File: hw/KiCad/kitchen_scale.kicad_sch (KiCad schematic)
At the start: 11 parts, among them J1 Conn_01x08_Socket, J2 Conn_HX711, SW1 SW_Push, SW2 SW_SPST, SW3 SW_Push, SW4 SW_Push, U1 DEBO1_3_7LI_1_0A charge_contr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, U2 WeMos_D1_mini, U3 LF33_TO220

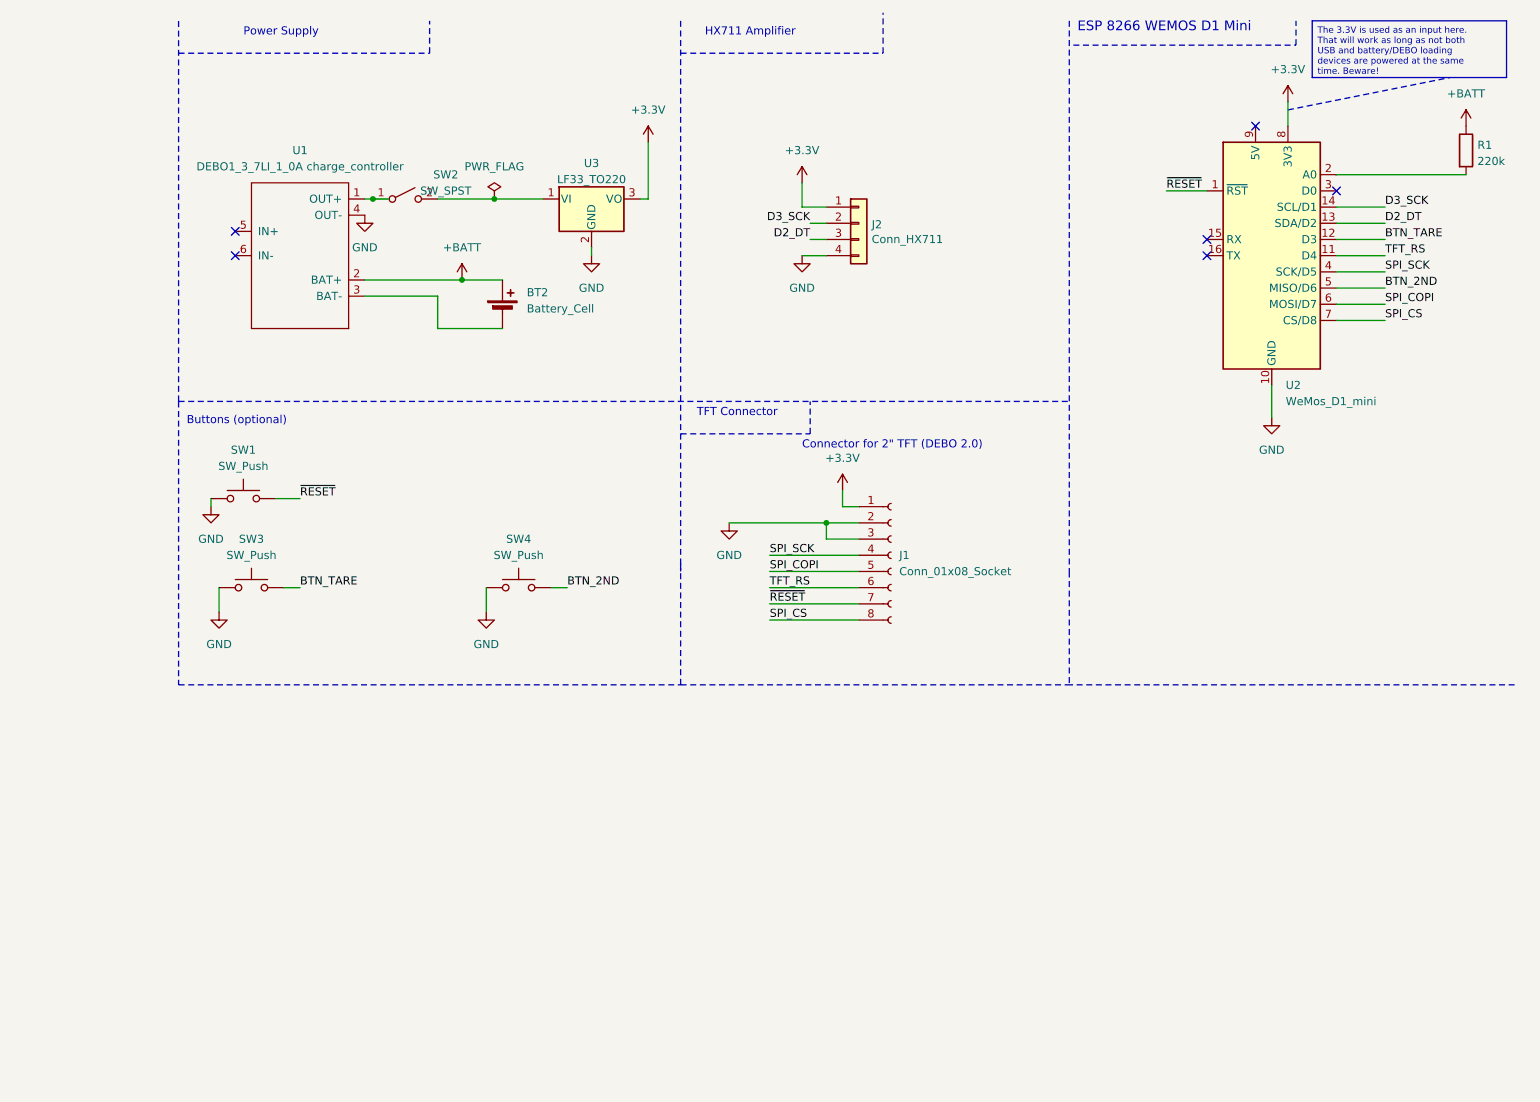
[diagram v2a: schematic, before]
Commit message: Add footprints Add first draft of PCB
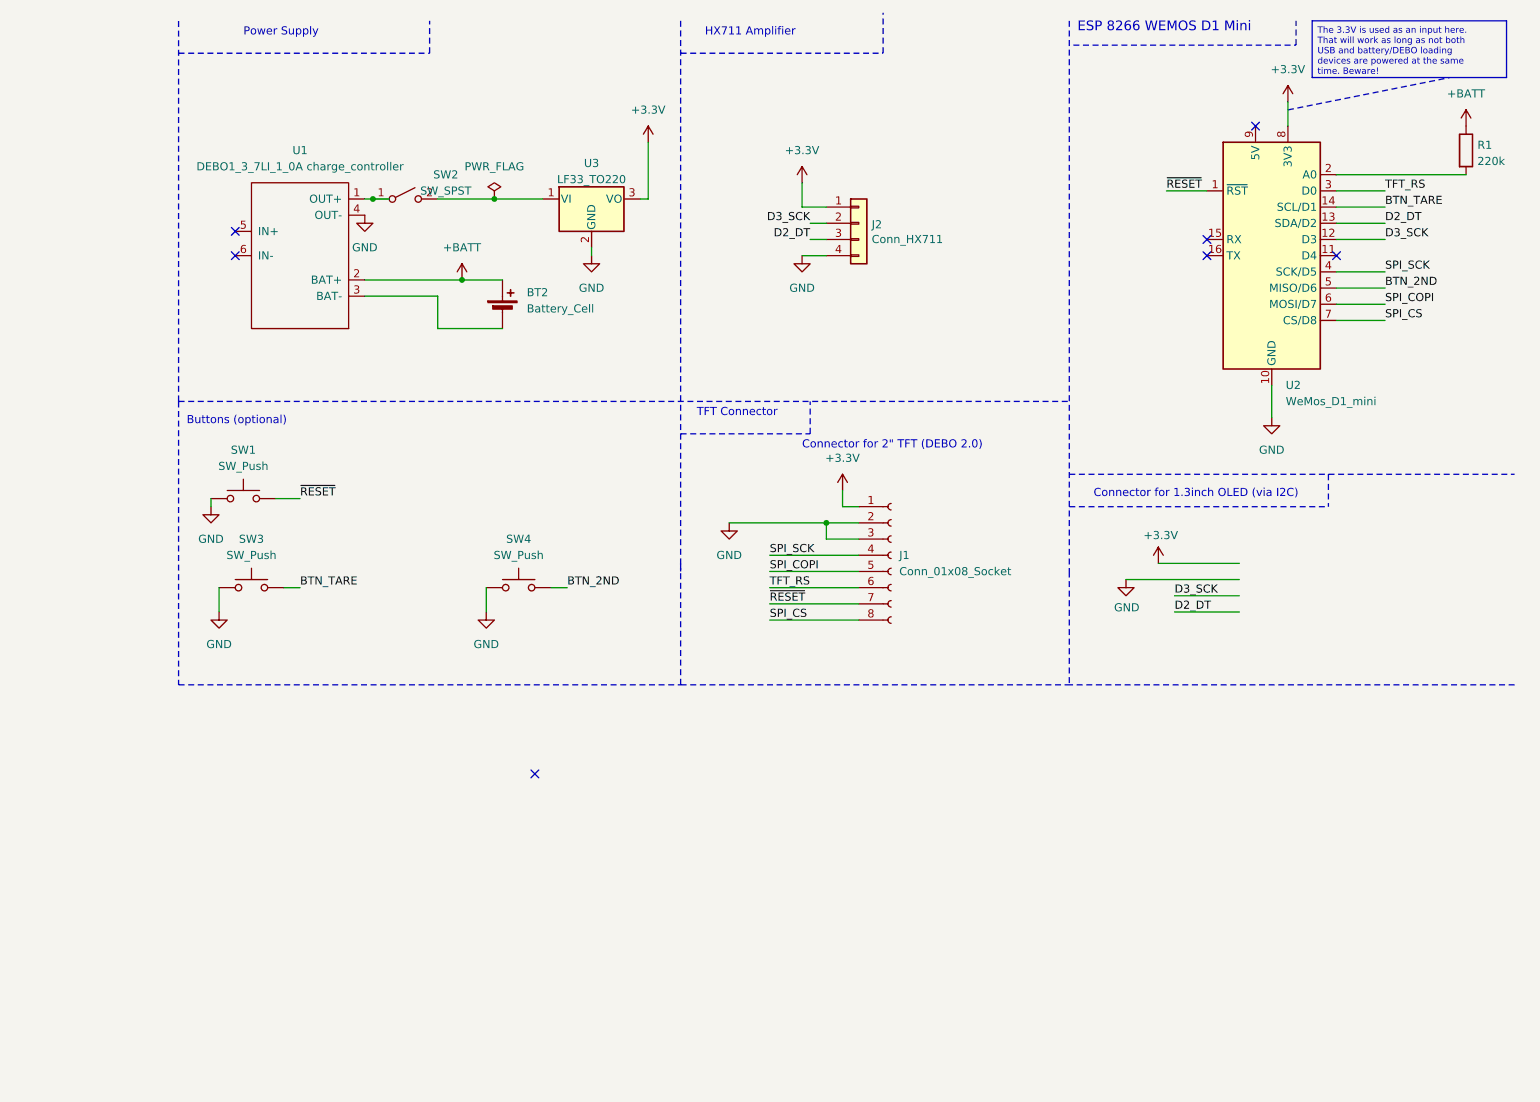
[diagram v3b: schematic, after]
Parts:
- BT2: footprint (none) -> Connector_PinHeader_2.54mm:PinHeader_1x02_P2.54mm_Vertical
- J1: footprint (none) -> Connector_PinHeader_2.54mm:PinHeader_2x04_P2.54mm_Vertical
- J2: footprint (none) -> Connector_PinSocket_2.54mm:PinSocket_1x04_P2.54mm_Vertical
- SW1, SW3, SW4: footprint (none) -> Button_Switch_THT:SW_PUSH-12mm
- SW2: footprint (none) -> Connector_PinSocket_2.54mm:PinSocket_1x02_P2.54mm_Vertical
- U1: footprint (none) -> Mine:DEBO1_3_7LI_1_0A_charge_controller
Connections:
- net BTN_TARE: now also U2.14 (SCL/D1); no longer U2.12 (D3)
- net D3_SCK: now also U2.12 (D3); no longer U2.14 (SCL/D1)
- net TFT_RS: now also U2.3 (D0); no longer U2.11 (D4)
- no-connect marks 6 -> 7
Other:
- note added: "Connector for 1.3inch OLED (via I2C)"
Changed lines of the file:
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@@
   )
   (no_connect (at 236.22 46.99))
-  (no_connect (at 256.54 39.37))
   (no_connect (at 243.84 29.21))
   (no_connect (at 236.22 49.53))
+  (no_connect (at 130.81 130.81))
   (no_connect (at 83.82 45.72))
   (no_connect (at 83.82 49.53))
+  (no_connect (at 256.54 49.53))
+  (wire (pts (xy 256.54 39.37) (xy 264.16 39.37))
+    (stroke (width 0) (type default))
+  )
   (polyline (pts (xy 153.67 12.7) (xy 153.67 99.06))
     (stroke (width 0) (type dash))
@@
     (stroke (width 0) (type default))
   )
+  (polyline (pts (xy 214.63 88.9) (xy 255.27 88.9))
+    (stroke (width 0) (type dash))
+  )
   (wire (pts (xy 167.64 106.68) (xy 181.61 106.68))
     (stroke (width 0) (type default))
@@
     (stroke (width 0) (type default))
   )
+  (wire (pts (xy 228.6 97.79) (xy 241.3 97.79))
+    (stroke (width 0) (type default))
+  )
   (wire (pts (xy 176.53 91.44) (xy 176.53 93.98))
     (stroke (width 0) (type default))
@@
   )
   (wire (pts (xy 167.64 96.52) (xy 181.61 96.52))
+    (stroke (width 0) (type default))
+  )
+  (wire (pts (xy 241.3 102.87) (xy 231.14 102.87))
     (stroke (width 0) (type default))
   )
@@
     (stroke (width 0) (type dash))
   )
+  (polyline (pts (xy 214.63 83.82) (xy 284.48 83.82))
+    (stroke (width 0) (type dash))
+  )
   (wire (pts (xy 81.28 101.6) (xy 81.28 105.41))
     (stroke (width 0) (type default))
@@
     (stroke (width 0) (type default))
   )
+  (wire (pts (xy 241.3 105.41) (xy 231.14 105.41))
+    (stroke (width 0) (type default))
+  )
   (wire (pts (xy 91.44 101.6) (xy 93.98 101.6))
     (stroke (width 0) (type default))
@@
     (stroke (width 0) (type dash))
   )
-  (wire (pts (xy 256.54 49.53) (xy 264.16 49.53))
-    (stroke (width 0) (type default))
-  )
   (wire (pts (xy 172.72 38.1) (xy 172.72 41.91))
     (stroke (width 0) (type default))
@@
     (stroke (width 0) (type default))
   )
+  (polyline (pts (xy 255.27 83.82) (xy 255.27 88.9))
+    (stroke (width 0) (type dash))
+  )
   (wire (pts (xy 115.57 40.64) (xy 124.46 40.64))
     (stroke (width 0) (type default))
@@
   (polyline (pts (xy 74.93 72.39) (xy 74.93 116.84))
     (stroke (width 0) (type dash))
+  )
+  (wire (pts (xy 223.52 100.33) (xy 241.3 100.33))
+    (stroke (width 0) (type default))
   )
   (polyline (pts (xy 214.63 99.06) (xy 214.63 116.84))
@@
     (effects (font (size 1.524 1.524)) (justify left bottom))
   )
+  (text "Connector for 1.3inch OLED (via I2C)" (at 218.44 87.63 0)
+    (effects (font (size 1.27 1.27)) (justify left bottom))
+  )
   (text "Buttons (optional)" (at 76.2 76.2 0)
     (effects (font (size 1.27 1.27)) (justify left bottom))
@@
   )
   (label "TFT_RS" (at 167.64 101.6 0) (fields_autoplaced)
+    (effects (font (size 1.27 1.27)) (justify left bottom))
+  )
+  (label "D2_DT" (at 231.14 105.41 0) (fields_autoplaced)
     (effects (font (size 1.27 1.27)) (justify left bottom))
   )
@@
     (effects (font (size 1.27 1.27)) (justify left bottom))
   )
-  (label "TFT_RS" (at 264.16 49.53 0) (fields_autoplaced)
-    (effects (font (size 1.27 1.27)) (justify left bottom))
-  )
-  (label "BTN_TARE" (at 264.16 46.99 0) (fields_autoplaced)
-    (effects (font (size 1.27 1.27)) (justify left bottom))
-  )
-  (label "D3_SCK" (at 264.16 41.91 0) (fields_autoplaced)
+  (label "TFT_RS" (at 264.16 39.37 0) (fields_autoplaced)
+    (effects (font (size 1.27 1.27)) (justify left bottom))
+  )
+  (label "BTN_TARE" (at 264.16 41.91 0) (fields_autoplaced)
+    (effects (font (size 1.27 1.27)) (justify left bottom))
+  )
+  (label "D3_SCK" (at 231.14 102.87 0) (fields_autoplaced)
+    (effects (font (size 1.27 1.27)) (justify left bottom))
+  )
+  (label "D3_SCK" (at 264.16 46.99 0) (fields_autoplaced)
     (effects (font (size 1.27 1.27)) (justify left bottom))
   )
@@
       (effects (font (size 1.27 1.27)) (justify left))
     )
-    (property "Footprint" "" (at 181.61 44.45 0)
+    (property "Footprint" "Connector_PinSocket_2.54mm:PinSocket_1x04_P2.54mm_Vertical" (at 181.61 44.45 0)
       (effects (font (size 1.27 1.27)) hide)
     )
@@
       (effects (font (size 1.27 1.27)))
     )
-    (property "Footprint" "" (at 110.49 40.64 0)
+    (property "Footprint" "Connector_PinSocket_2.54mm:PinSocket_1x02_P2.54mm_Vertical" (at 110.49 40.64 0)
       (effects (font (size 1.27 1.27)) hide)
     )
@@
       (effects (font (size 1.27 1.27)) (justify left))
     )
-    (property "Footprint" "" (at 125.73 56.896 90)
+    (property "Footprint" "Connector_PinHeader_2.54mm:PinHeader_1x02_P2.54mm_Vertical" (at 125.73 56.896 90)
       (effects (font (size 1.27 1.27)) hide)
     )
@@
     )
   )
+  (symbol (lib_id "power:+3.3V") (at 228.6 97.79 0) (unit 1)
+    (in_bom yes) (on_board yes) (dnp no)
+    (property "Reference" "#PWR018" (at 228.6 101.6 0)
+      (effects (font (size 1.27 1.27)) hide)
+    )
+    (property "Value" "+3.3V" (at 228.981 93.3958 0)
+      (effects (font (size 1.27 1.27)))
+    )
+    (property "Footprint" "" (at 228.6 97.79 0)
+      (effects (font (size 1.27 1.27)) hide)
+    )
+    (property "Datasheet" "" (at 228.6 97.79 0)
+      (effects (font (size 1.27 1.27)) hide)
+    )
+    (pin "1")
+    (instances
+      (project "kitchen_scale"
+        (path "/cef6f603-8a0b-4dd0-af99-ebfbef7d1b4b"
+          (reference "#PWR018") (unit 1)
+        )
+      )
+    )
+  )
   (symbol (lib_id "Switch:SW_Push") (at 86.36 101.6 0) (unit 1)
     (in_bom yes) (on_board yes) (dnp no) (fields_autoplaced)
@@
       (effects (font (size 1.27 1.27)))
     )
-    (property "Footprint" "" (at 86.36 96.52 0)
+    (property "Footprint" "Button_Switch_THT:SW_PUSH-12mm" (at 86.36 96.52 0)
       (effects (font (size 1.27 1.27)) hide)
     )
@@
     )
   )
+  (symbol (lib_id "power:GND") (at 223.52 100.33 0) (unit 1)
+    (in_bom yes) (on_board yes) (dnp no)
+    (property "Reference" "#PWR017" (at 223.52 106.68 0)
+      (effects (font (size 1.27 1.27)) hide)
+    )
+    (property "Value" "GND" (at 223.647 104.7242 0)
+      (effects (font (size 1.27 1.27)))
+    )
+    (property "Footprint" "" (at 223.52 100.33 0)
+      (effects (font (size 1.27 1.27)) hide)
+    )
+    (property "Datasheet" "" (at 223.52 100.33 0)
+      (effects (font (size 1.27 1.27)) hide)
+    )
+    (pin "1")
+    (instances
+      (project "kitchen_scale"
+        (path "/cef6f603-8a0b-4dd0-af99-ebfbef7d1b4b"
+          (reference "#PWR017") (unit 1)
+        )
+      )
+    )
+  )
   (symbol (lib_id "Mine:DEBO1_3_7LI_1_0A_charge_controller") (at 93.98 62.23 0) (unit 1)
     (in_bom yes) (on_board yes) (dnp no) (fields_autoplaced)
@@
       (effects (font (size 1.27 1.27)))
     )
-    (property "Footprint" "" (at 93.98 62.23 0)
+    (property "Footprint" "Mine:DEBO1_3_7LI_1_0A_charge_controller" (at 93.98 62.23 0)
       (effects (font (size 1.27 1.27)) hide)
     )
@@
       (effects (font (size 1.27 1.27)))
     )
-    (property "Footprint" "" (at 85.09 82.55 0)
+    (property "Footprint" "Button_Switch_THT:SW_PUSH-12mm" (at 85.09 82.55 0)
       (effects (font (size 1.27 1.27)) hide)
     )
@@
       (effects (font (size 1.27 1.27)) (justify left))
     )
-    (property "Footprint" "" (at 186.69 96.52 0)
+    (property "Footprint" "Connector_PinHeader_2.54mm:PinHeader_2x04_P2.54mm_Vertical" (at 186.69 96.52 0)
       (effects (font (size 1.27 1.27)) hide)
     )
@@
       (effects (font (size 1.27 1.27)))
     )
-    (property "Footprint" "" (at 128.27 96.52 0)
-      (effects (font (size 1.27 1.27)) hide)
-    )
+    (property "Footprint" "Button_Switch_THT:SW_PUSH-12mm" (at 128.27 96.52 0)
+      (effects (font (size 1.27 1.27)) hide)
+    )

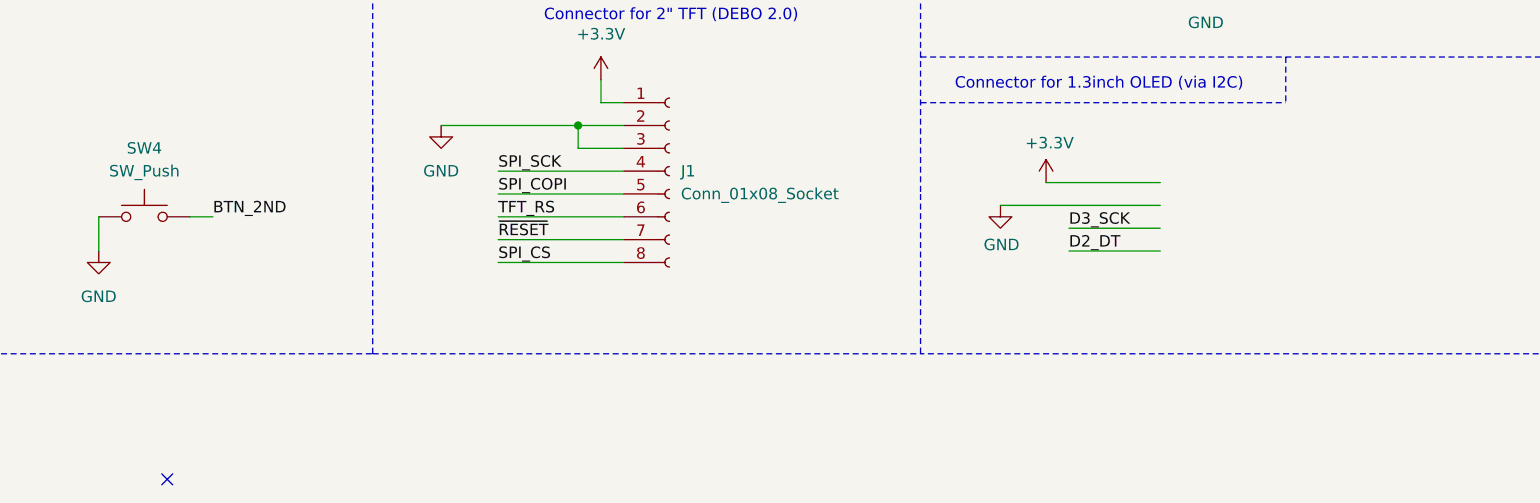
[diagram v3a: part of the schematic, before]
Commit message: Completed wiring
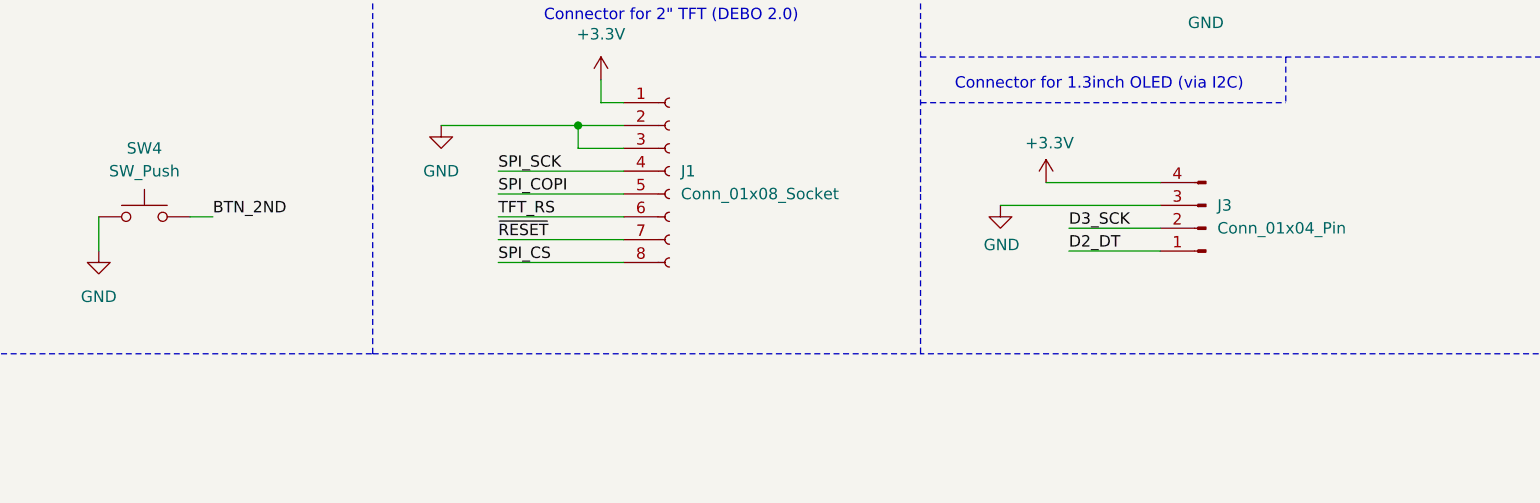
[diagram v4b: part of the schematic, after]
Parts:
- added J3: Conn_01x04_Pin, Connector_PinHeader_2.54mm:PinHeader_1x04_P2.54mm_Vertical, symbol Connector:Conn_01x04_Pin
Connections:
- net +3.3V: now also J3.4 (Pin_4)
- net D2_DT: now also J3.1 (Pin_1)
- net D3_SCK: now also J3.2 (Pin_2)
- net GND: now also J3.3 (Pin_3)
- no-connect marks 7 -> 6
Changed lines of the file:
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@@
   (no_connect (at 243.84 29.21))
   (no_connect (at 236.22 49.53))
-  (no_connect (at 130.81 130.81))
   (no_connect (at 83.82 45.72))
   (no_connect (at 83.82 49.53))
@@
     (stroke (width 0) (type default))
   )
-  (wire (pts (xy 228.6 97.79) (xy 241.3 97.79))
-    (stroke (width 0) (type default))
-  )
   (wire (pts (xy 176.53 91.44) (xy 176.53 93.98))
     (stroke (width 0) (type default))
@@
     (stroke (width 0) (type default))
   )
-  (wire (pts (xy 241.3 102.87) (xy 231.14 102.87))
+  (wire (pts (xy 231.14 102.87) (xy 241.3 102.87))
     (stroke (width 0) (type default))
   )
@@
   )
   (wire (pts (xy 248.92 25.4) (xy 248.92 29.21))
+    (stroke (width 0) (type default))
+  )
+  (wire (pts (xy 228.6 97.79) (xy 241.3 97.79))
     (stroke (width 0) (type default))
   )
@@
         )
       )
+    )
+  )
+  (symbol (lib_id "Connector:Conn_01x04_Pin") (at 246.38 102.87 180) (unit 1)
+    (in_bom yes) (on_board yes) (dnp no) (fields_autoplaced)
+    (property "Reference" "J3" (at 247.65 100.33 0)
+      (effects (font (size 1.27 1.27)) (justify right))
+    )
+    (property "Value" "Conn_01x04_Pin" (at 247.65 102.87 0)
+      (effects (font (size 1.27 1.27)) (justify right))
+    )
+    (property "Footprint" "Connector_PinHeader_2.54mm:PinHeader_1x04_P2.54mm_Vertical" (at 246.38 102.87 0)
+      (effects (font (size 1.27 1.27)) hide)
+    )
+    (property "Datasheet" "~" (at 246.38 102.87 0)
+      (effects (font (size 1.27 1.27)) hide)
+    )
+    (pin "3")
+    (pin "2")
+    (pin "1")
+    (pin "4")
+    (instances
+      (project "kitchen_scale"
+        (path "/cef6f603-8a0b-4dd0-af99-ebfbef7d1b4b"
+          (reference "J3") (unit 1)
+        )
+      )
